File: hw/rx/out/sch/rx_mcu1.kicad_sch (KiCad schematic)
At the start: 21 parts, among them J2 SWD, U1 BT40NE

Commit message: hw/rx: review fixes for #81 (mute relay + supervisor, S1J clamps, VCM discharge + 2-pole filter, 16 V LDOs, keyed header, I2S DNP, cable stability + power-cycle SPICE, FLT low latency) (#32)
Co-Authored-By: Claude Opus 5.5 <noreply@anthropic.com>
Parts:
- R33, R34, R35: value 100 -> DNP (100); DNP (none) -> yes; MPN R_0402_1% -> DNP
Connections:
- net OUT_EN: now reaches U1.12 (P0.11)
- net DAC_XSMT renamed XSMT_EN
- no-connect marks 40 -> 39
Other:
- moved on the sheet: C10, C11, C12, J2, R20, R21, R22, R23, R24, R25, R26, R27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

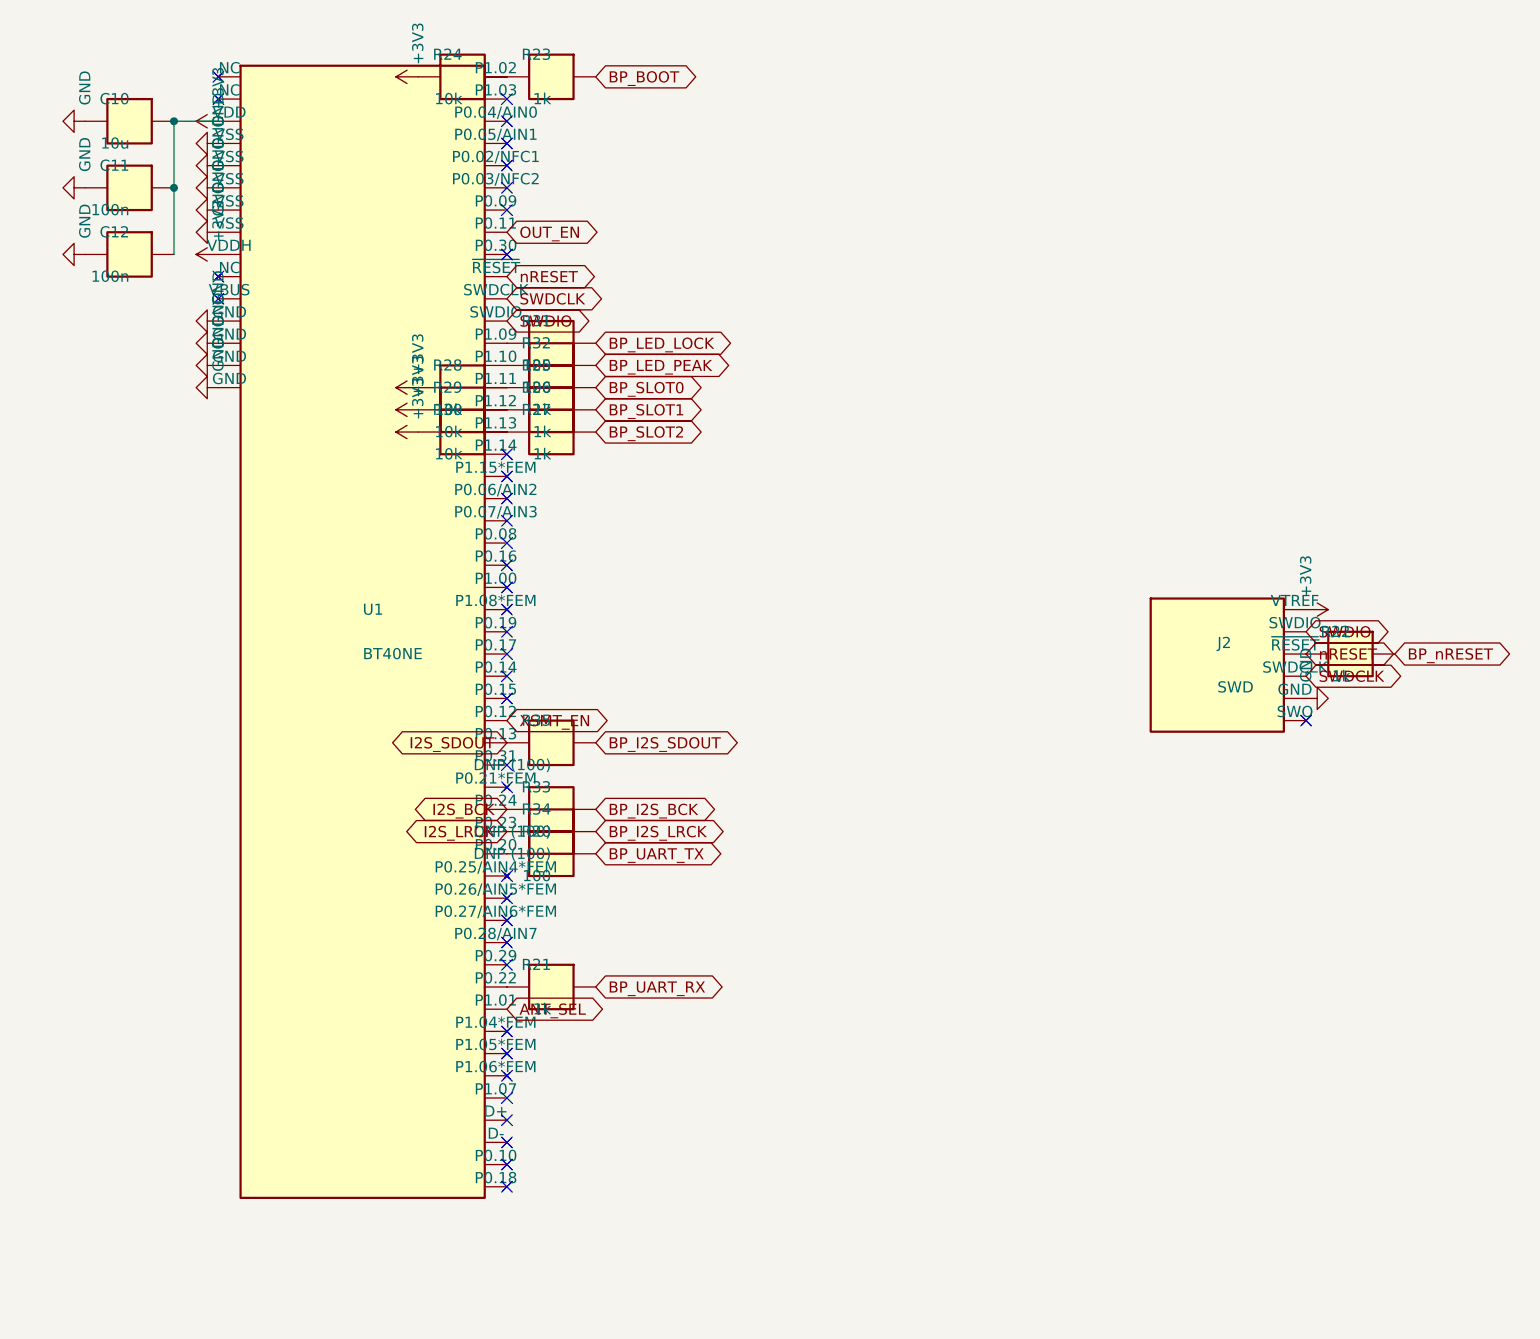
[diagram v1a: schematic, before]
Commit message: hw/rx: receiver module BT40NE -> BT40E, FEM node pack-only (ADR-0021, #112)
- hw/rx: BT40E symbol (Fanstel v1.09 p.14 pad map = BT40F/NE names), footprint
  openpack:Fanstel_BT40E (14x16 mm), no FEM nets, P1.05 open; GPIO map unchanged.
  ERC 0/0. BOM: Digi-Key UK GBP 9.7765 q100 -> $30.68 / GBP 23.38 per sub-board.
- fw: receiver builds add boards/role_rx_cpunet.overlay (FEM node disabled, no
  &radio fem); rx.c refuses to build with the FEM enabled.
- ADR-0014 amended (datasheet checks, FCC X8WBT40F, no UKCA DoC, BOM).

Co-Authored-By: Claude Opus 5.5 <noreply@anthropic.com>
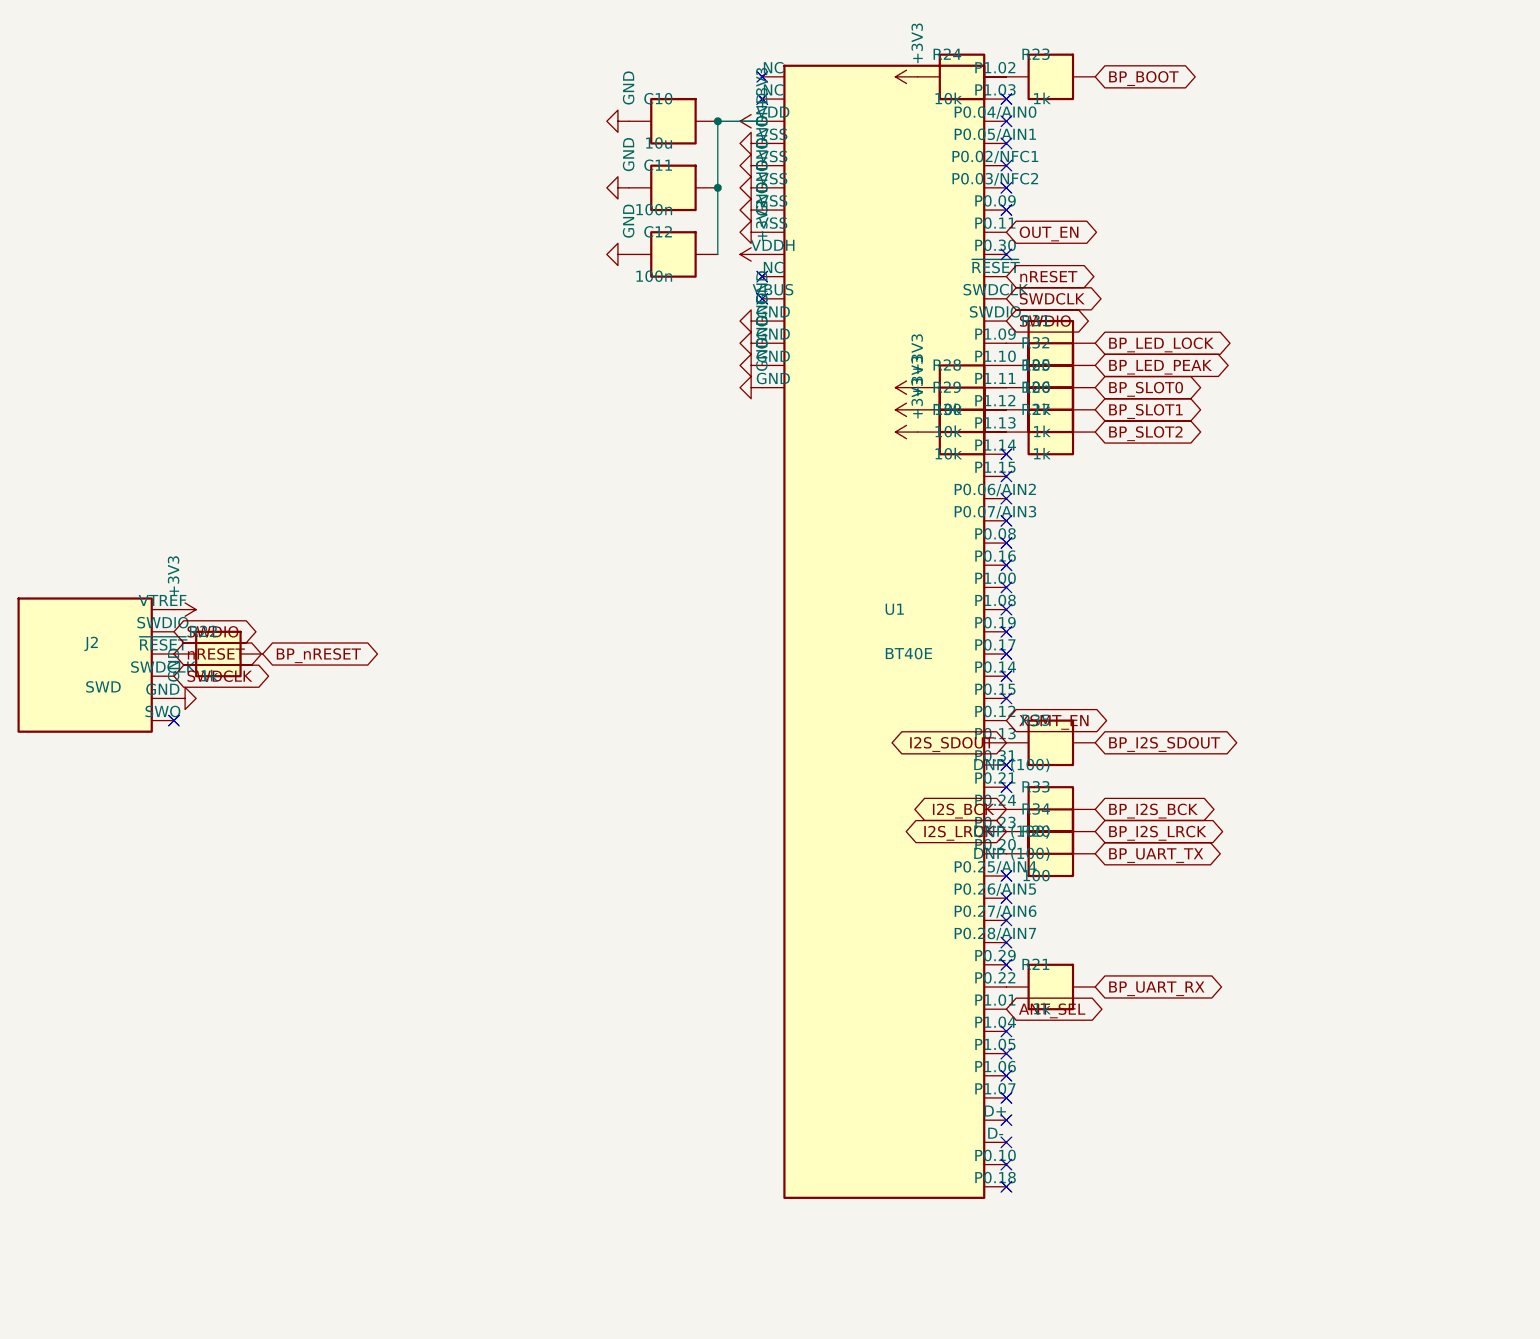
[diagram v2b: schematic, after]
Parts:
- U1: value BT40NE -> BT40E; footprint openpack:Fanstel_BT40NE -> openpack:Fanstel_BT40E; symbol openpack_rx:BT40NE -> openpack_rx:BT40E; MPN BT40NE -> BT40E
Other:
- moved on the sheet: C10, C11, C12, J2, R20, R21, R22, R23, R24, R25, R26, R27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

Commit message: hw/rx: receiver sub-board layout, 50 ohm GCPW, keyed J1, JLC rules that load, fab outputs (#34) (#116)
Part of #34. Receiver layout (48x90 mm, DRC 0/0), #116 independent-review fixes (netclass pour clearances in rx + pack, no hole at J1 pin 14, solid RF grounds, K1 pin-1/CPL), every placed part with a checked LCSC code.

Co-Authored-By: Claude Opus 5.5 <noreply@anthropic.com>
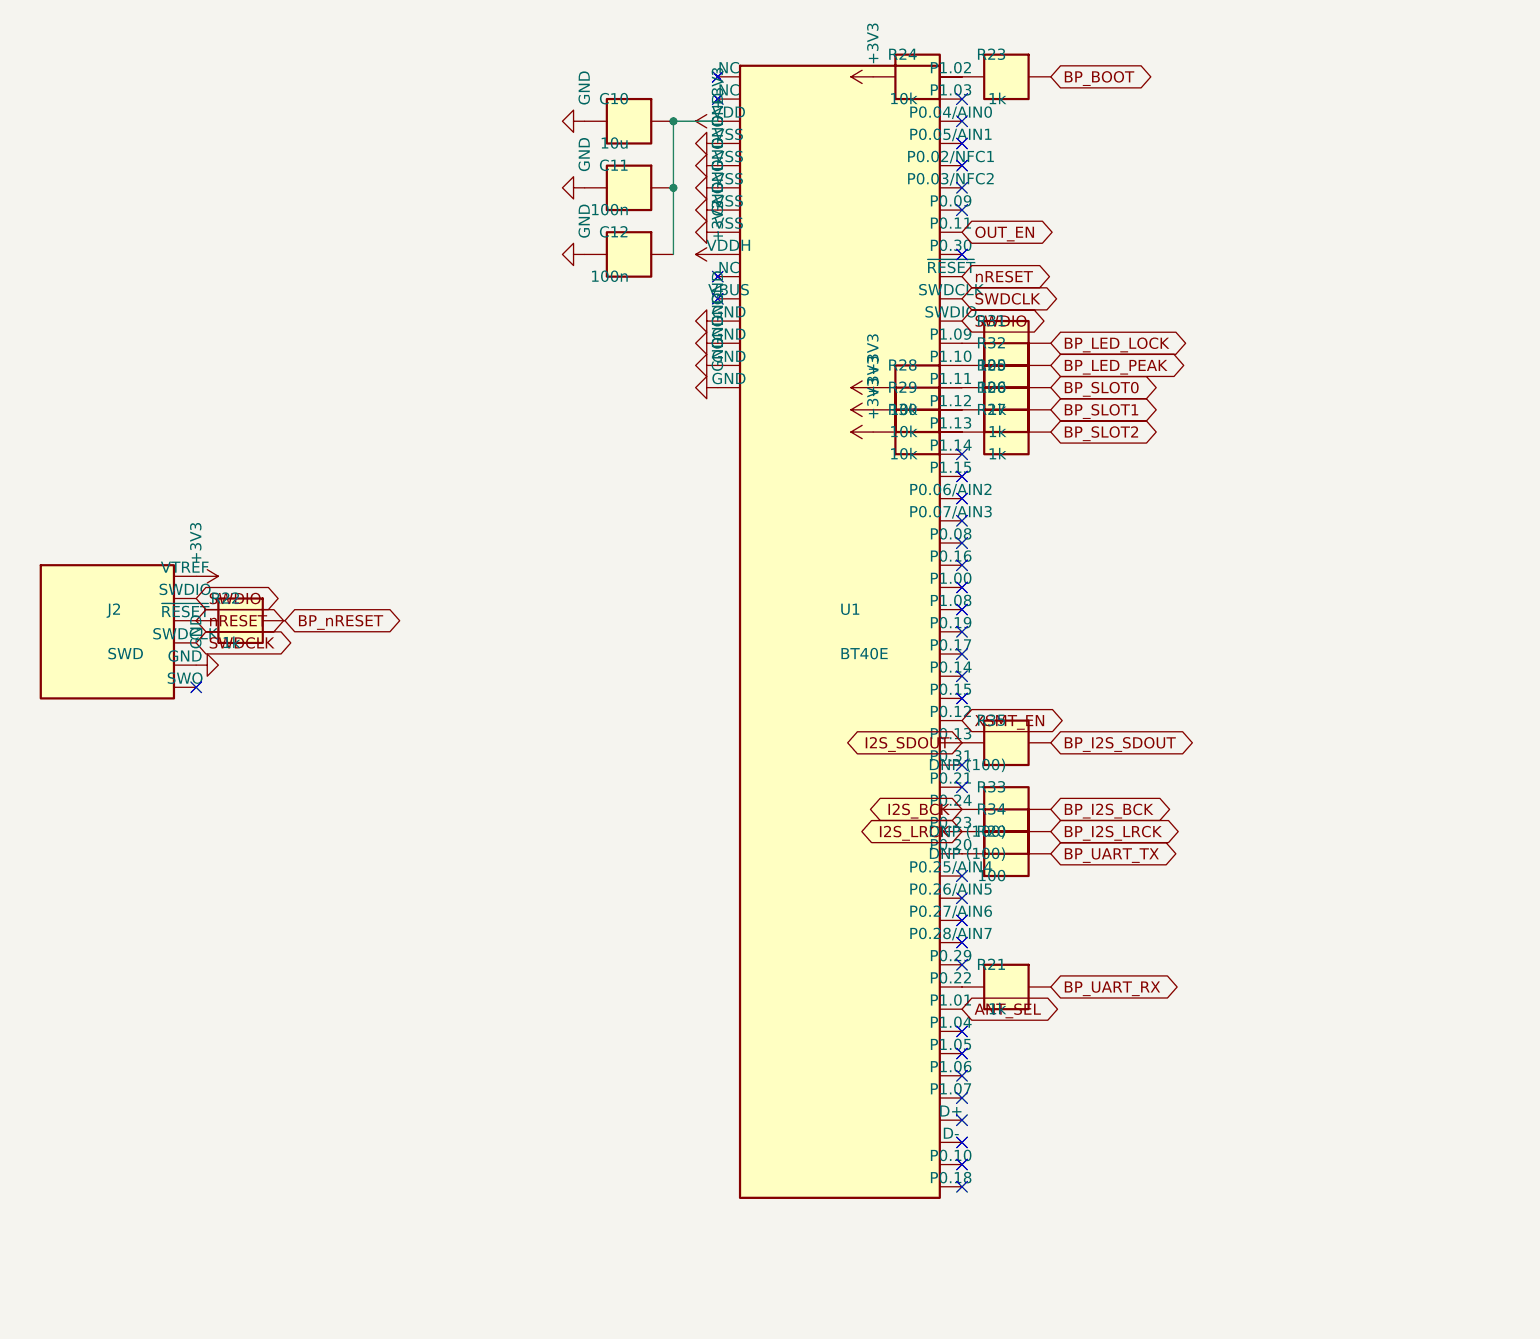
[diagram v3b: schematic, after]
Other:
- moved on the sheet: C10, C11, C12, J2, R20, R21, R22, R23, R24, R25, R26, R27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
